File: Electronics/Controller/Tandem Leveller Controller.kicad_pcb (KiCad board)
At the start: 2 copper layers, 136 parts, among them J1 Conn_01x02, J10 CAN BUS, J11 TRACTOR BATTERY, J12 PWR SWITCH, J13 VALVE POWER, J14 TABLET 1 PWR, J15 TABLET 2 PWR, J16 SLAVE TABLET, J17 MASTER TABLET, J18 292303-7, J19 292303-7, J2 GPS SIM, J20 FRONT HEIGHT, J21 REAR HEIGHT, J22 SWITCHES, J3 Conn_01x02, J4 Conn_01x02, J5 Conn_01x02, J6 Conn_01x02, J7 Conn_01x02, J8 Conn_01x02, J9 TERM, U1 TEENSY 4.0, U10 FT232RL, U11 FT232RL, U12 FT232RL, U13 FT232RL, U14 FT232RL, U15 FT232RL, U16 USB2517, U17 MIC2026-1YM, U2 simpleRTK2B, U3 simpleRTK2B, U4 simpleRTK2B, U5 TJA1462ATK-0Z, U6 PESD2CANFD24V-TR, U7 LM2596S-5, U8 LM2587S-ADJ/NOPB, U9 LM2587S-ADJ/NOPB, Y1 FA-238 24.0000MD30X-W5

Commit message: Working on PCB layout.
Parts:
- moved J1 495.8 mm to (108.4, 85.9), turned to 0 degrees
- moved R16 485.7 mm to (117.9, 81.0), turned to -90 degrees
- moved U1 484.5 mm to (111.7, 100.9), turned to 90 degrees
- moved C16 484.2 mm to (124.5, 68.4), turned to 0 degrees
- moved C18 482.9 mm to (120.0, 81.0), turned to -90 degrees
- moved U13 482.6 mm to (123.0, 74.3), turned to 90 degrees
- moved R17 480.2 mm to (122.1, 81.0), turned to -90 degrees
- moved J20 470.2 mm to (120.5, 106.4), turned to 180 degrees
- moved R40 468.9 mm to (133.4, 74.6), turned to -90 degrees
- moved R39 466.3 mm to (135.4, 74.6), turned to -90 degrees
- moved R38 453.4 mm to (145.4, 74.6), turned to -90 degrees
- moved J21 452.4 mm to (133.7, 106.4), turned to 180 degrees
- moved R37 450.8 mm to (147.4, 74.6), turned to -90 degrees
- moved R36 448.1 mm to (149.5, 74.6), turned to -90 degrees
- moved J22 434.9 mm to (157.4, 79.8), turned to 180 degrees
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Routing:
- net +12V: track 191.3 -> 188.4 mm
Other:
- board outline added: 212 x 146.5 mm
- board text added: "PRI TABLET"
- board text added: "SEC TABLET"

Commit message: Working on PCB layout.
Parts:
- added J23: CAN, EmSA:DB9_RA_MALE_LD09P13A4, F.Cu at (265.9, 57.0)
- moved J10 127.7 mm to (219.9, 44.3), turned to 0 degrees
- moved R3 127.1 mm to (226.8, 48.7), turned to 0 degrees
- moved J9 125.7 mm to (229.5, 51.6), turned to -90 degrees
- moved U6 122.4 mm to (221.7, 49.5), turned to 180 degrees
- moved L1 118.5 mm to (223.7, 53.9), turned to 90 degrees
- moved R2 115.3 mm to (221.1, 55.0), turned to -90 degrees
- moved C2 115.1 mm to (226.2, 58.5), turned to -90 degrees
- moved J3 114.5 mm to (244.2, 165.8), turned to 180 degrees
- moved J1 113.9 mm to (217.8, 54.2), turned to -90 degrees
- moved R40 111.9 mm to (245.2, 69.5), turned to 180 degrees
- moved C1 110.9 mm to (225.5, 61.6), turned to 0 degrees
- moved C16 110.9 mm to (235.3, 70.2), turned to -90 degrees
- moved U5 110.7 mm to (222.6, 59.8), turned to 0 degrees
- moved R39 109.8 mm to (245.2, 71.5), turned to 180 degrees
- moved J6 107.6 mm to (244.2, 159.5), turned to 180 degrees
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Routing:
- added copper zone on B.Cu, net GND
- added copper zone on F.Cu, net GND
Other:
- board size 212 x 146.5 mm -> 212 x 145 mm

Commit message: Working on PCB layout.
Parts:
- moved R27 18.6 mm to (186.6, 59.6), turned to -90 degrees
- moved C28 3.72 mm to (184.2, 48.8)
- moved C30 3.61 mm to (182.0, 48.8)
- moved C35 2.08 mm to (179.8, 48.8)
- moved C37 0.50 mm to (174.0, 47.6)
- moved C38 0.50 mm to (176.5, 47.6)
- moved R29 0.50 mm to (171.9, 47.6)
- turned C26 to 0 degrees
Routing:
- net +5V: track 43.0 -> 674.2 mm, vias 4 -> 38
- net /USB Devices/GNSS_REAR_D+: track 0.00 -> 184.1 mm, vias 0 -> 6
- net /USB Devices/GNSS_REAR_D-: track 0.00 -> 184.0 mm, vias 0 -> 6
- net /GNSS/GNSS_TRACTOR_TX: track 0.00 -> 182.7 mm, vias 0 -> 4
- net /USB Devices/GNSS_TRACTOR_D+: track 0.00 -> 182.0 mm, vias 0 -> 6
- net /USB Devices/GNSS_TRACTOR_D-: track 0.00 -> 181.6 mm, vias 0 -> 6
- net /GNSS/GNSS_TRACTOR_RX: track 0.00 -> 180.0 mm, vias 0 -> 5
- net /USB Devices/GNSS_FRONT_D-: track 0.00 -> 148.0 mm, vias 0 -> 6
- net /USB Devices/GNSS_FRONT_D+: track 0.00 -> 146.0 mm, vias 0 -> 6
- net /GNSS/GNSS_REAR_TX: track 0.00 -> 131.5 mm, vias 0 -> 3
- net /GNSS/GNSS_REAR_RX: track 0.00 -> 123.3 mm, vias 0 -> 3
- net /GNSS/GNSS_FRONT_RX: track 0.00 -> 121.8 mm, vias 0 -> 4
- net /USB Devices/ARDUINO_D+: track 0.00 -> 119.6 mm, vias 0 -> 8
- net /GNSS/GNSS_FRONT_TX: track 0.00 -> 117.0 mm, vias 0 -> 3
- net /USB Devices/ARDUINO_D-: track 0.00 -> 113.6 mm, vias 0 -> 8
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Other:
- outline, holes or cut-outs redrawn
- board text added: "CAN"
- board text added: "CAN TERM"
- board text added: "CONTROLS"
- board text added: "ENABLE"
- board text added: "FRONT"
- board text added: "FRONT ROVER"
- board text added: "GNSS SIM"
- board text added: "REAR"
- board text added: "REAR ROVER"
- board text added: "TABLET PWR 16V"
- board text added: "TANDEM SCRAPER GNSS CONTROLLER (C) ANDY@BRITISHIDEAS.COM 2025 VERSION 1.0"
- board text added: "TRACTOR ROVER"

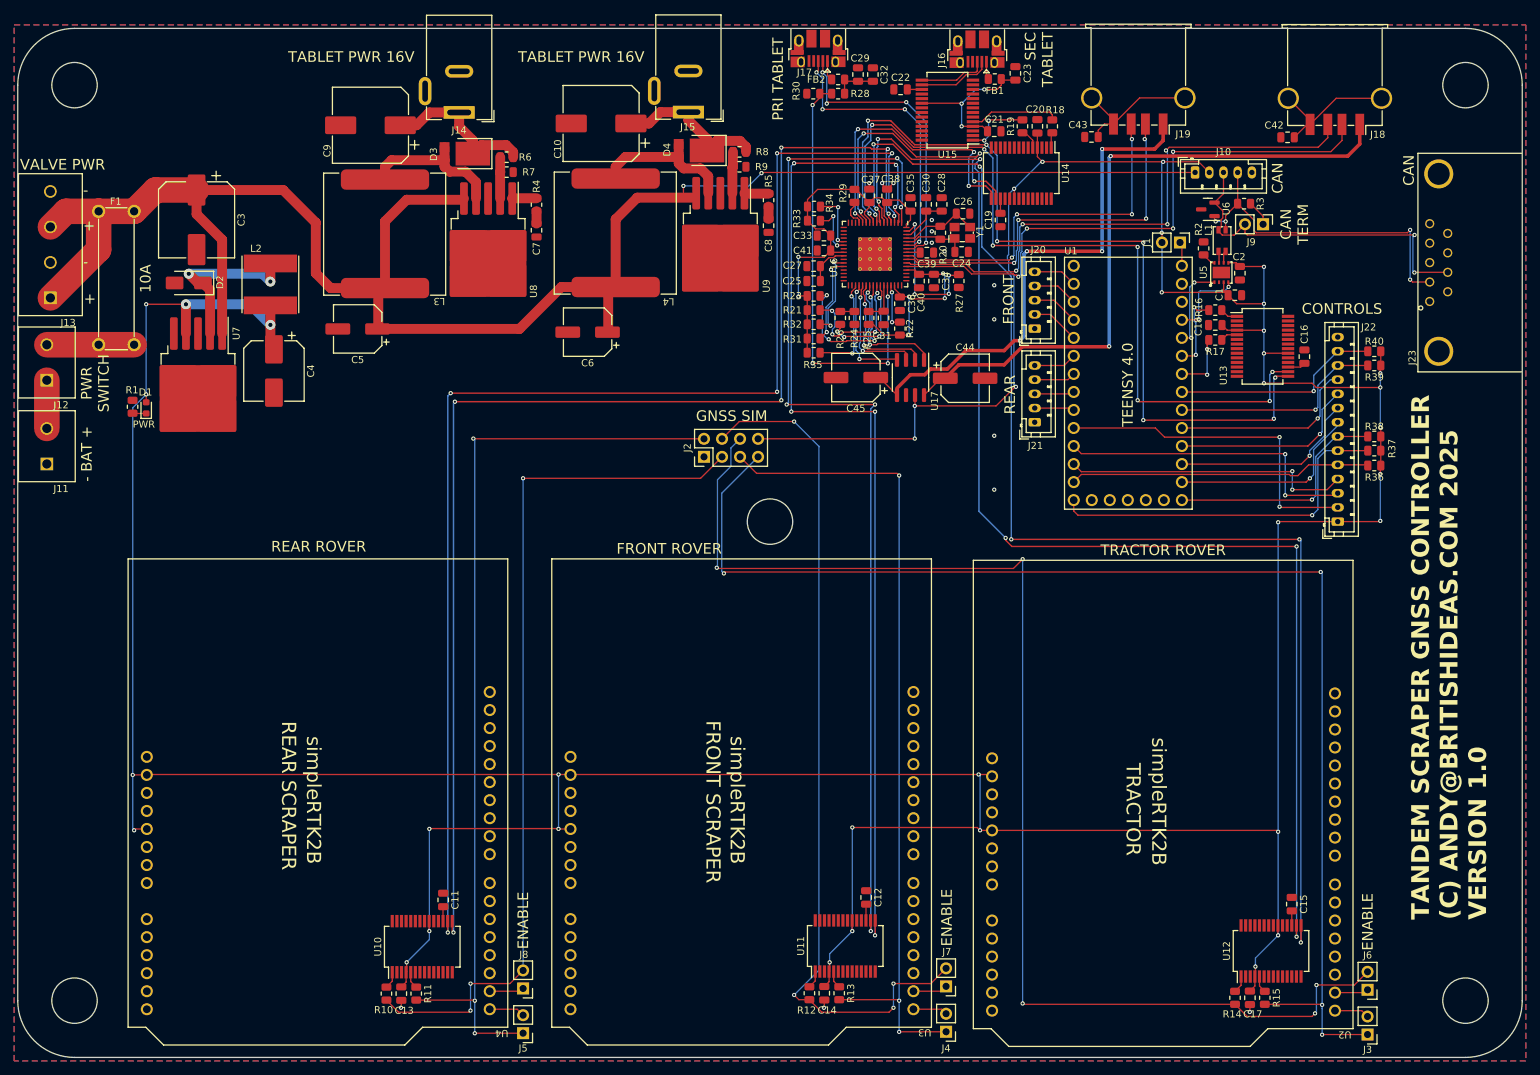
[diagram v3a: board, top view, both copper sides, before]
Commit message: First attempt at PCB layout completed.
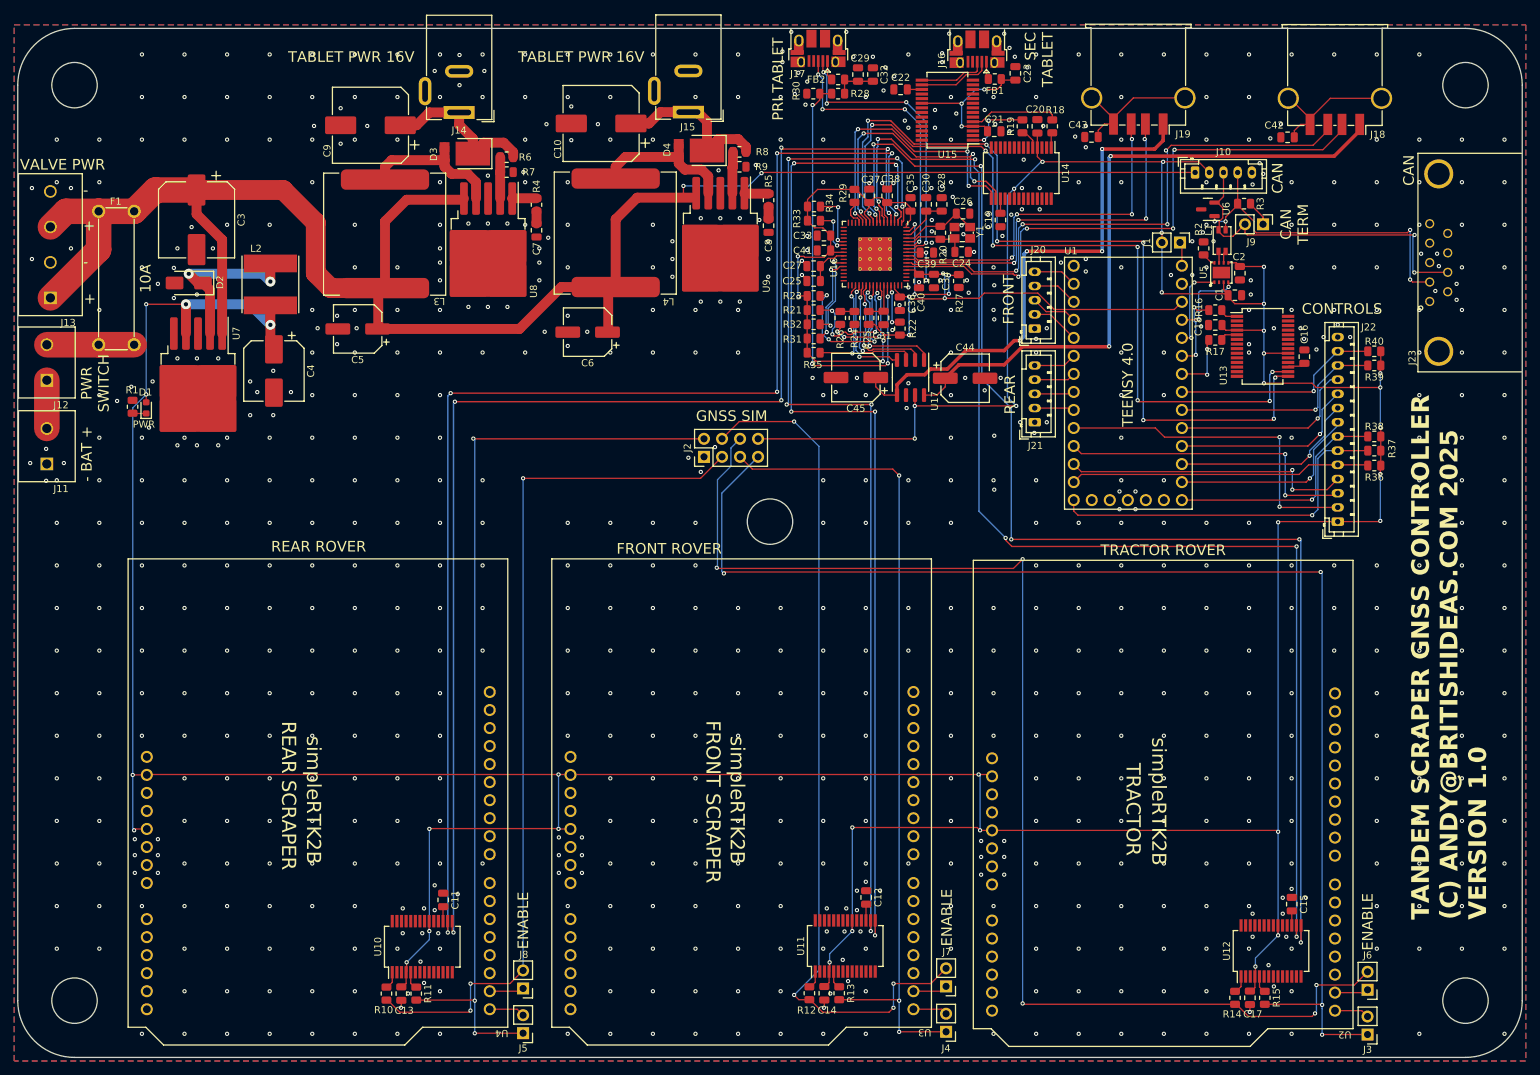
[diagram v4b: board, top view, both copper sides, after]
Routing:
- net +3V3: track 88.2 -> 144.7 mm, vias 6 -> 10
- net GND: track 6.48 -> 9.72 mm, vias 14 -> 825
- net +5V: track 674.2 -> 676.4 mm
- net /Slave Tablet/SLAVE_TABLET_D-: track 40.5 -> 39.2 mm
- net /Slave Tablet/SLAVE_TABLET_D+: track 41.2 -> 40.1 mm
- net /USB Hub/VBUS7: track 74.5 -> 75.6 mm
- net /Power/16V_2: track 22.4 -> 23.3 mm
- net Net-(U16-OSC3_N): track 7.36 -> 6.40 mm
- net /USB Devices/GNSS_TRACTOR_D-: track 181.6 -> 180.7 mm
- net /USB Devices/GNSS_FRONT_D-: track 148.0 -> 147.4 mm
- net Net-(J19-GND): track 20.0 -> 20.6 mm
- net Net-(J18-D+): track 79.3 -> 78.7 mm
- net Net-(U16-VBUS_DET): track 61.7 -> 62.3 mm
- net Net-(J18-D-): track 81.8 -> 81.3 mm

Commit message: Reduced size of bolt holes on controller. Started work on IMU.
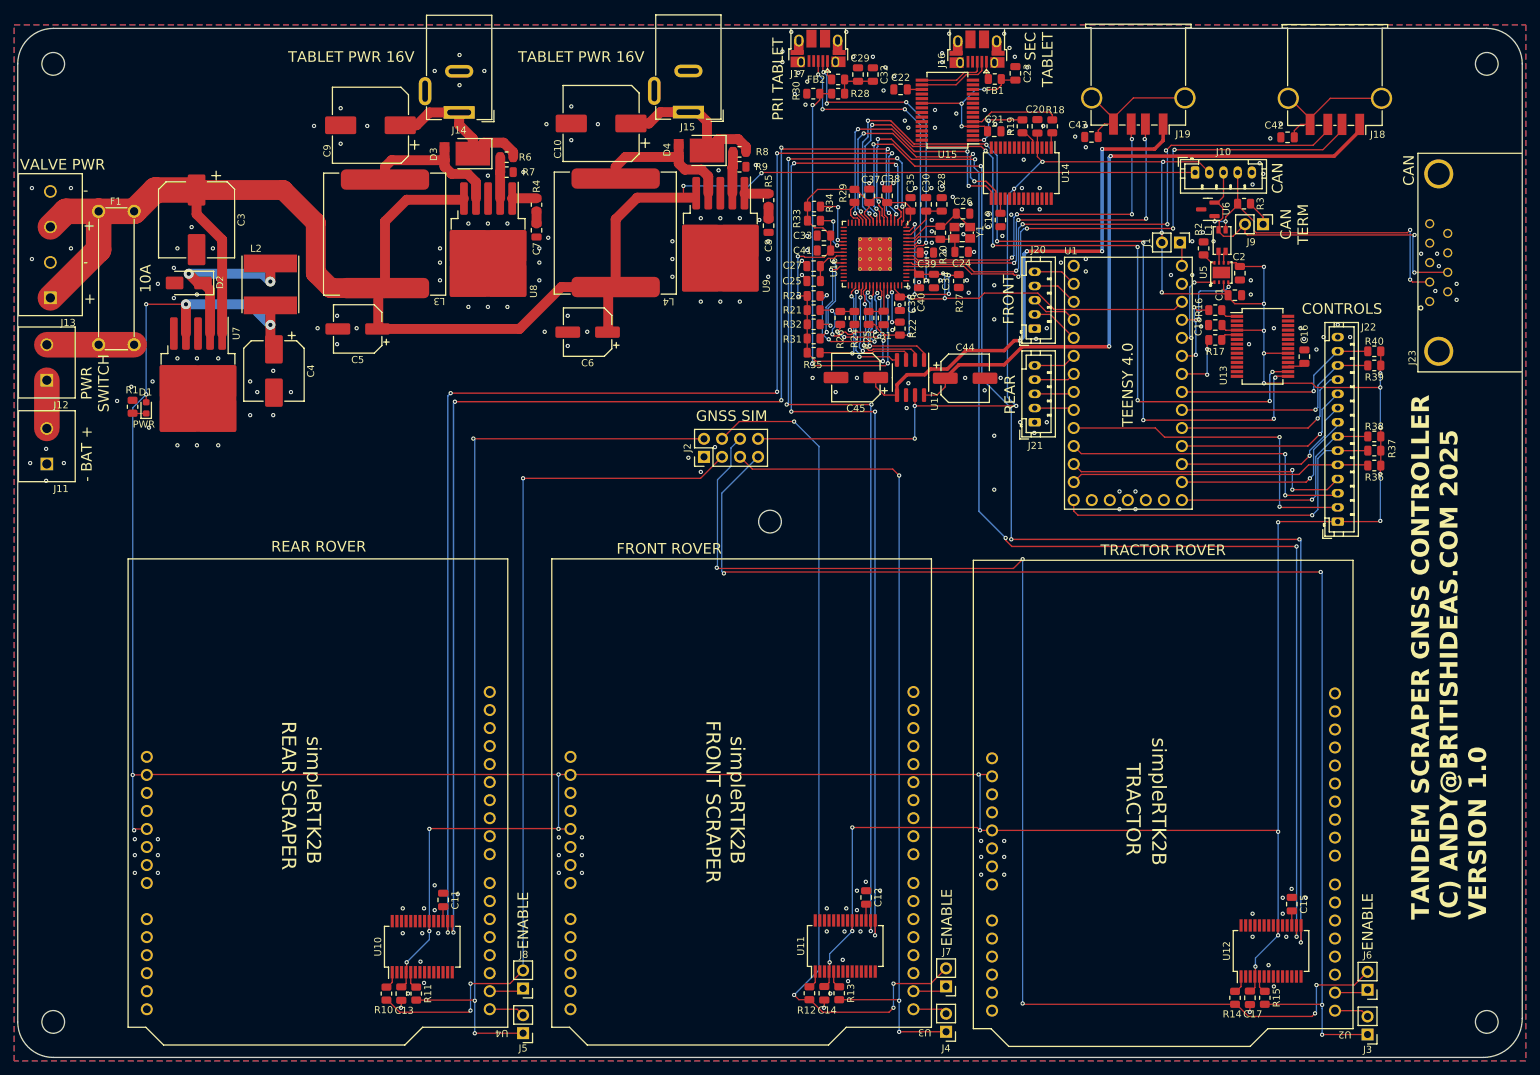
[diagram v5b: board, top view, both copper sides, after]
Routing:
- net GND: vias 825 -> 257
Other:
- outline, holes or cut-outs redrawn
